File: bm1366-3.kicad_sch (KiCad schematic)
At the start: 77 parts, among them U1 25MHz, U21 TLV3544, U23 AP7331, U24 AP7331, U25 BM1368_mode1, U27 BM1368_mode1

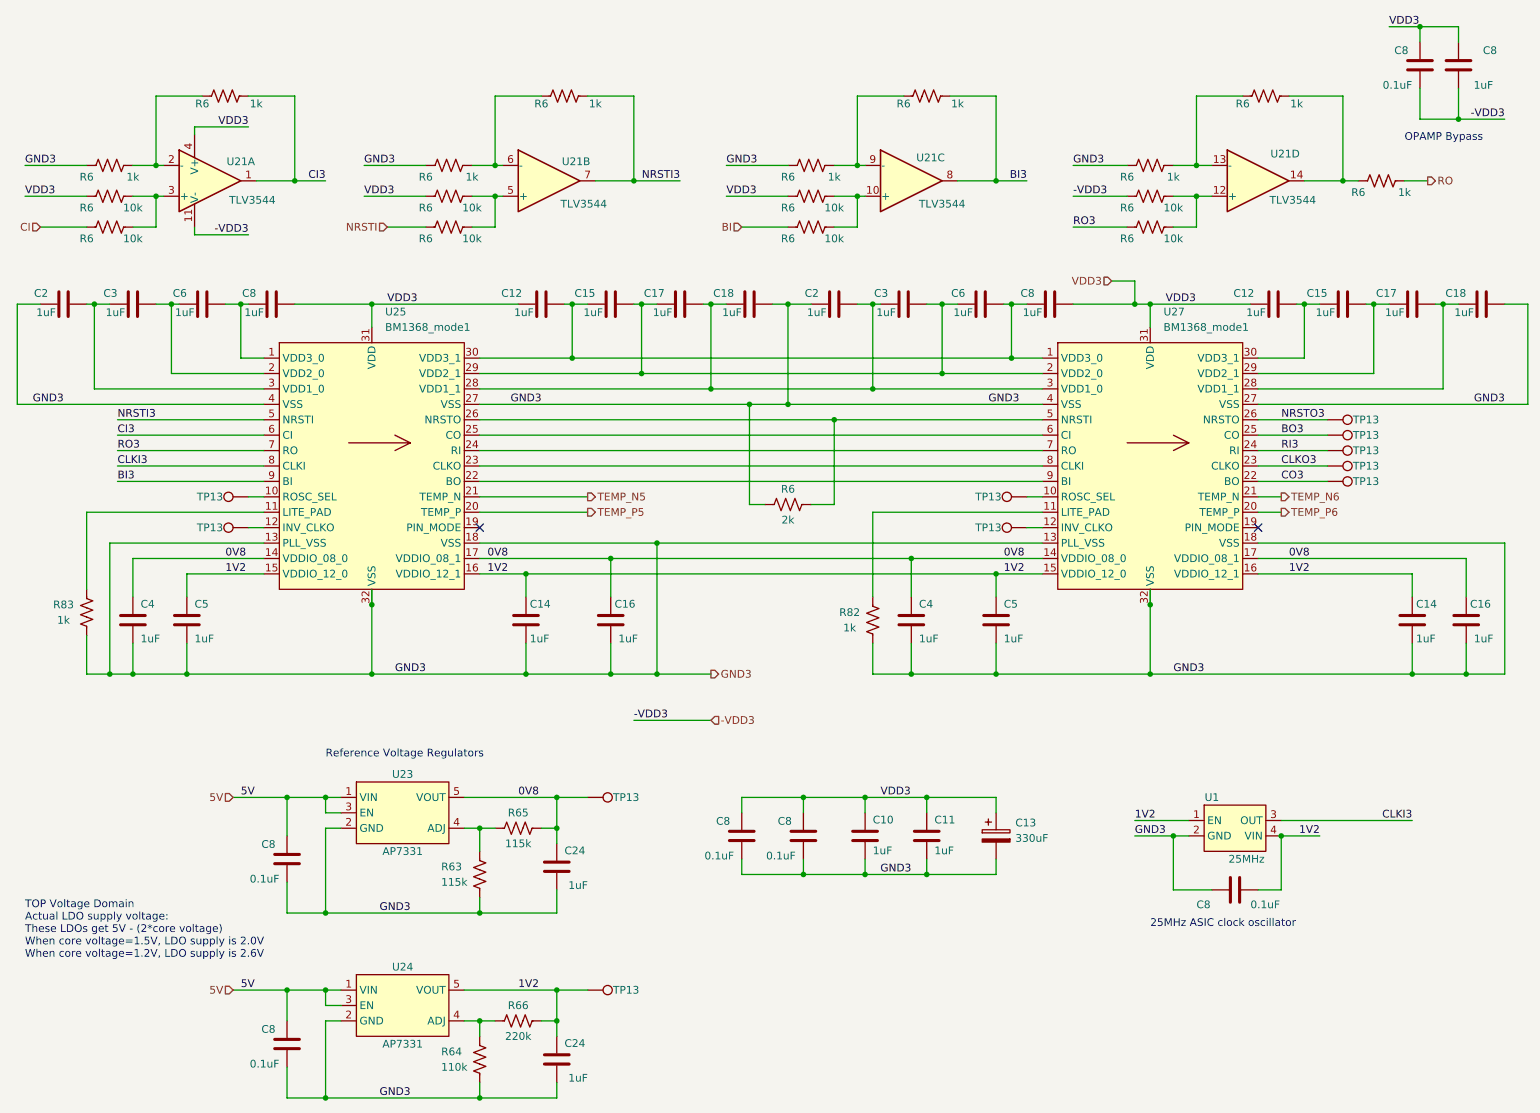
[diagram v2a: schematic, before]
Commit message: Reset to 1V8
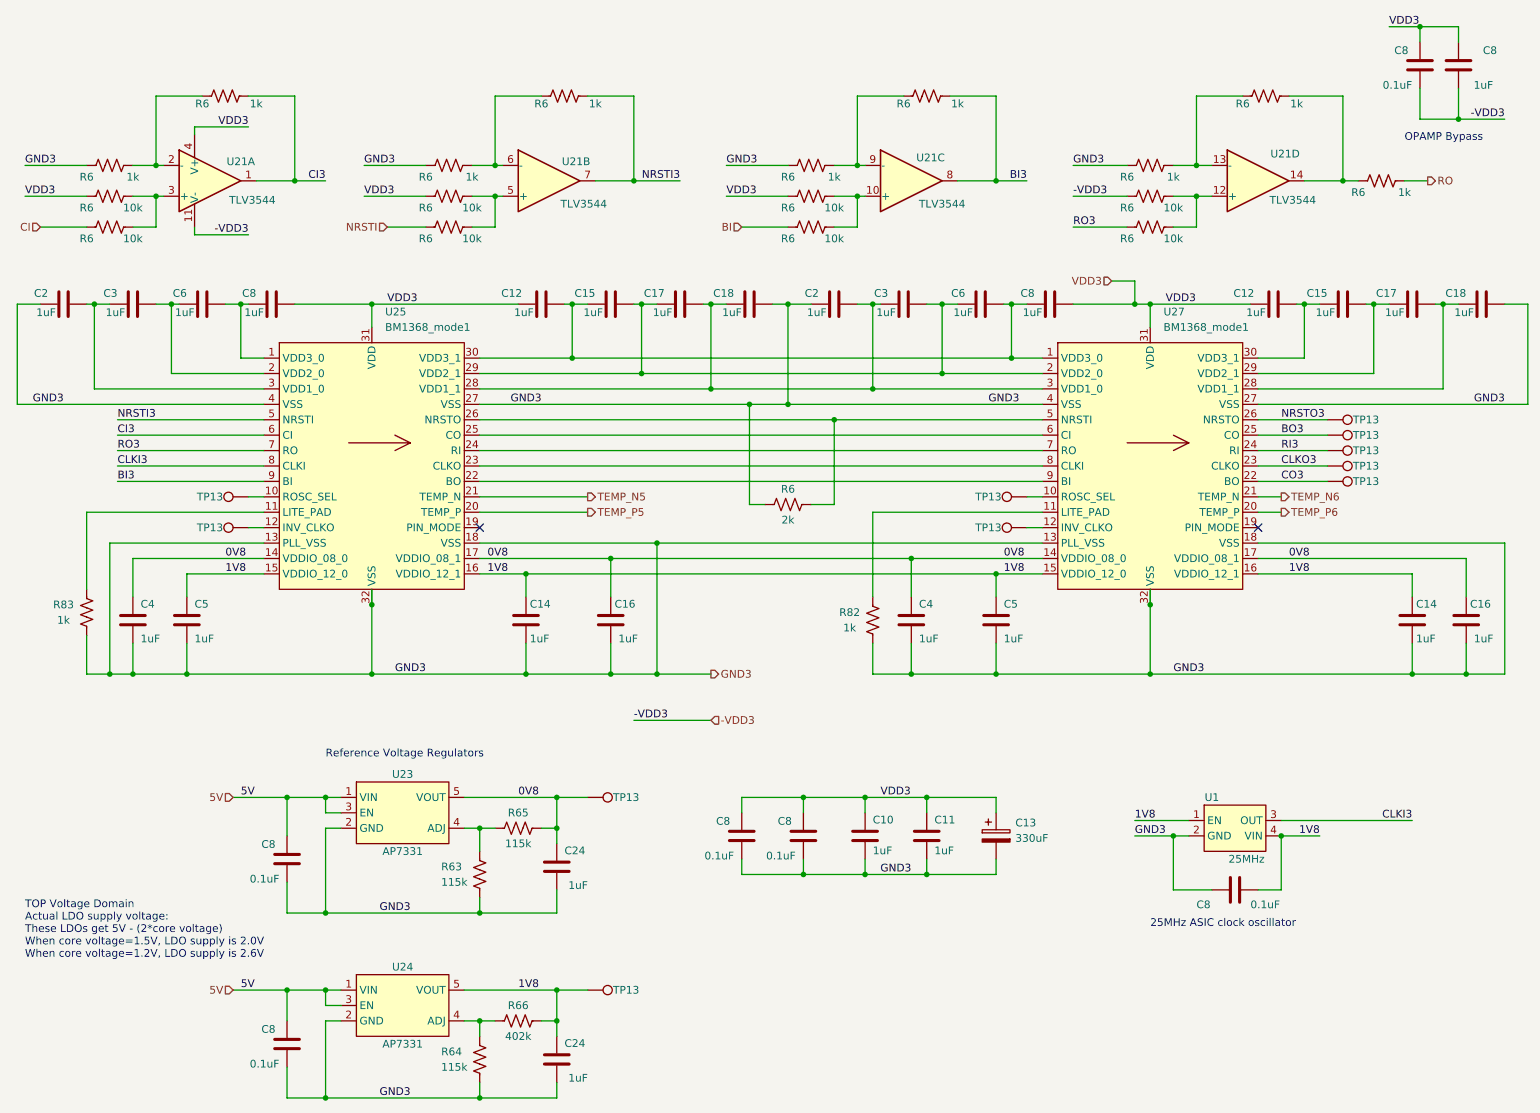
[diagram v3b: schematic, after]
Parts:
- R64: value 110k -> 115k; DK 311-110KLRTR-ND -> YAG2956CT-ND; PARTNO RC0402FR-07110KL -> RC0402FR-07115KL
- R66: value 220k -> 402k; DK 311-220KLRTR-ND -> YAG3151CT-ND; PARTNO RC0402FR-07220KL -> RC0402FR-07402KL
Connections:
- net 1V2 renamed 1V8
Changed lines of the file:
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@@
 		)
 	)
-	(label "1V2"
+	(label "1V8"
 		(at 229.87 151.13 180)
 		(fields_autoplaced yes)
@@
 		)
 	)
-	(label "1V2"
+	(label "1V8"
 		(at 49.53 107.95 0)
 		(fields_autoplaced yes)
@@
 		)
 	)
-	(label "1V2"
+	(label "1V8"
 		(at 224.79 107.95 0)
 		(fields_autoplaced yes)
@@
 		)
 	)
-	(label "1V2"
+	(label "1V8"
 		(at 92.71 107.95 0)
 		(fields_autoplaced yes)
@@
 		)
 	)
-	(label "1V2"
+	(label "1V8"
 		(at 177.8 107.95 0)
 		(fields_autoplaced yes)
@@
 		)
 	)
-	(label "1V2"
+	(label "1V8"
 		(at 199.39 148.59 0)
 		(fields_autoplaced yes)
@@
 		)
 	)
-	(label "1V2"
+	(label "1V8"
 		(at 97.79 176.53 0)
 		(fields_autoplaced yes)
@@
 	)
 	(symbol
+		(lib_id "Device:R_US")
+		(at 97.79 181.61 270)
+		(unit 1)
+		(exclude_from_sim no)
+		(in_bom yes)
+		(on_board yes)
+		(dnp no)
+		(property "Reference" "R66"
+			(at 97.79 179.07 90)
+			(effects
+				(font
+					(size 1.27 1.27)
+				)
+			)
+		)
+		(property "Value" "402k"
+			(at 97.79 184.15 90)
+			(effects
+				(font
+					(size 1.27 1.27)
+				)
+			)
+		)
+		(property "Footprint" "Resistor_SMD:R_0402_1005Metric"
+			(at 97.536 182.626 90)
+			(effects
+				(font
+					(size 1.27 1.27)
+				)
+				(hide yes)
+			)
+		)
+		(property "Datasheet" "~"
+			(at 97.79 181.61 0)
+			(effects
+				(font
+					(size 1.27 1.27)
+				)
+				(hide yes)
+			)
+		)
+		(property "Description" ""
+			(at 97.79 181.61 0)
+			(effects
+				(font
+					(size 1.27 1.27)
+				)
+				(hide yes)
+			)
+		)
+		(property "DK" "YAG3151CT-ND"
+			(at 97.79 181.61 0)
+			(effects
+				(font
+					(size 1.27 1.27)
+				)
+				(hide yes)
+			)
+		)
+		(property "PARTNO" "RC0402FR-07402KL"
+			(at 97.79 181.61 0)
+			(effects
+				(font
+					(size 1.27 1.27)
+				)
+				(hide yes)
+			)
+		)
+		(pin "1"
+		)
+		(pin "2"
+		)
+		(instances
+			(project "bitaxeHex"
+				(path "/e63e39d7-6ac0-4ffd-8aa3-1841a4541b55/e182566a-9202-4486-8792-212410a9233c"
+					(reference "R66")
+					(unit 1)
+				)
+			)
+		)
+	)
+	(symbol
 		(lib_id "Device:C")
 		(at 104.14 187.96 0)
@@
 	)
 	(symbol
-		(lib_id "Device:R_US")
-		(at 97.79 181.61 270)
-		(unit 1)
-		(exclude_from_sim no)
-		(in_bom yes)
-		(on_board yes)
-		(dnp no)
-		(property "Reference" "R66"
-			(at 97.79 179.07 90)
-			(effects
-				(font
-					(size 1.27 1.27)
-				)
-			)
-		)
-		(property "Value" "220k"
-			(at 97.79 184.15 90)
-			(effects
-				(font
-					(size 1.27 1.27)
-				)
-			)
-		)
-		(property "Footprint" "Resistor_SMD:R_0402_1005Metric"
-			(at 97.536 182.626 90)
-			(effects
-				(font
-					(size 1.27 1.27)
-				)
-				(hide yes)
-			)
-		)
-		(property "Datasheet" "~"
-			(at 97.79 181.61 0)
-			(effects
-				(font
-					(size 1.27 1.27)
-				)
-				(hide yes)
-			)
-		)
-		(property "Description" ""
-			(at 97.79 181.61 0)
-			(effects
-				(font
-					(size 1.27 1.27)
-				)
-				(hide yes)
-			)
-		)
-		(property "DK" "311-220KLRTR-ND"
-			(at 97.79 181.61 0)
-			(effects
-				(font
-					(size 1.27 1.27)
-				)
-				(hide yes)
-			)
-		)
-		(property "PARTNO" "RC0402FR-07220KL"
-			(at 97.79 181.61 0)
-			(effects
-				(font
-					(size 1.27 1.27)
-				)
-				(hide yes)
-			)
-		)
-		(pin "1"
-		)
-		(pin "2"
-		)
-		(instances
-			(project "bitaxeHex"
-				(path "/e63e39d7-6ac0-4ffd-8aa3-1841a4541b55/e182566a-9202-4486-8792-212410a9233c"
-					(reference "R66")
-					(unit 1)
-				)
-			)
-		)
-	)
-	(symbol
 		(lib_id "Device:C")
 		(at 101.6 63.5 90)
@@
 	(symbol
 		(lib_id "Device:R_US")
+		(at 91.44 187.96 180)
+		(unit 1)
+		(exclude_from_sim no)
+		(in_bom yes)
+		(on_board yes)
+		(dnp no)
+		(property "Reference" "R64"
+			(at 85.09 186.69 0)
+			(effects
+				(font
+					(size 1.27 1.27)
+				)
+				(justify right)
+			)
+		)
+		(property "Value" "115k"
+			(at 85.09 189.23 0)
+			(effects
+				(font
+					(size 1.27 1.27)
+				)
+				(justify right)
+			)
+		)
+		(property "Footprint" "Resistor_SMD:R_0402_1005Metric"
+			(at 90.424 187.706 90)
+			(effects
+				(font
+					(size 1.27 1.27)
+				)
+				(hide yes)
+			)
+		)
+		(property "Datasheet" "~"
+			(at 91.44 187.96 0)
+			(effects
+				(font
+					(size 1.27 1.27)
+				)
+				(hide yes)
+			)
+		)
+		(property "Description" ""
+			(at 91.44 187.96 0)
+			(effects
+				(font
+					(size 1.27 1.27)
+				)
+				(hide yes)
+			)
+		)
+		(property "DK" "YAG2956CT-ND"
+			(at 91.44 187.96 0)
+			(effects
+				(font
+					(size 1.27 1.27)
+				)
+				(hide yes)
+			)
+		)
+		(property "PARTNO" "RC0402FR-07115KL"
+			(at 91.44 187.96 0)
+			(effects
+				(font
+					(size 1.27 1.27)
+				)
+				(hide yes)
+			)
+		)
+		(pin "1"
+		)
+		(pin "2"
+		)
+		(instances
+			(project "bitaxeHex"
+				(path "/e63e39d7-6ac0-4ffd-8aa3-1841a4541b55/e182566a-9202-4486-8792-212410a9233c"
+					(reference "R64")
+					(unit 1)
+				)
+			)
+		)
+	)
+	(symbol
+		(lib_id "Device:R_US")
 		(at 105.41 29.21 270)
 		(unit 1)
@@
 					(unit 1)
 				)
-			)
-		)
-	)
-	(symbol
-		(lib_id "Device:R_US")
-		(at 91.44 187.96 180)
-		(unit 1)
-		(exclude_from_sim no)
-		(in_bom yes)
-		(on_board yes)
-		(dnp no)
-		(property "Reference" "R64"
-			(at 85.09 186.69 0)
-			(effects
-				(font
-					(size 1.27 1.27)
-				)
-				(justify right)
-			)
-		)
-		(property "Value" "110k"
-			(at 85.09 189.23 0)
-			(effects
-				(font
-					(size 1.27 1.27)
-				)
-				(justify right)
-			)
-		)
-		(property "Footprint" "Resistor_SMD:R_0402_1005Metric"
-			(at 90.424 187.706 90)
-			(effects
-				(font
-					(size 1.27 1.27)
-				)
-				(hide yes)
-			)
-		)
-		(property "Datasheet" "~"
-			(at 91.44 187.96 0)
-			(effects
-				(font
-					(size 1.27 1.27)
-				)
-				(hide yes)
-			)
-		)
-		(property "Description" ""
-			(at 91.44 187.96 0)
-			(effects
-				(font
-					(size 1.27 1.27)
-				)
-				(hide yes)
-			)
-		)
-		(property "DK" "311-110KLRTR-ND"
-			(at 91.44 187.96 0)
-			(effects
-				(font
-					(size 1.27 1.27)
-				)
-				(hide yes)
-			)
-		)
-		(property "PARTNO" "RC0402FR-07110KL"
-			(at 91.44 187.96 0)
-			(effects
-				(font
-					(size 1.27 1.27)
-				)
-				(hide yes)
-			)
-		)
-		(pin "1"
-		)
-		(pin "2"
-		)
-		(instances
-			(project "bitaxeHex"
-				(path "/e63e39d7-6ac0-4ffd-8aa3-1841a4541b55/e182566a-9202-4486-8792-212410a9233c"
-					(reference "R64")
-					(unit 1)
-				)

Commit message: init push for GammaHex
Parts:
- removed U25, U27: BM1368_mode1, bitaxe:BM1368, symbol bitaxe:BM1368_mode1
- added U25, U27: BM1370_mode1, bitaxe:BM1370, symbol bitaxe:BM1370_mode1
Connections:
- net 0V8: now also U25.14 (VDDIO_08_0), U25.17 (VDDIO_08_1), U27.14 (VDDIO_08_0), U27.17 (VDDIO_08_1)
- net 1V8: now also U25.15 (VDDIO_12_0), U25.16 (VDDIO_12_1), U27.15 (VDDIO_12_0), U27.16 (VDDIO_12_1)
- net BI3: now also U25.9 (BI)
- net BO3: now also U27.25 (CO)
- net CI3: now also U25.6 (CI)
- net CLKI3: now also U25.8 (CLKI)
- net CLKO3: now also U27.23 (CLKO)
- net CO3: now also U27.22 (BO)
- net GND3: now also U25.13 (PLL_VSS), U25.18 (VSS), U25.27 (VSS), U25.32 (VSS), U25.4 (VSS), U27.13 (PLL_VSS), U27.18 (VSS), U27.27 (VSS), U27.32 (VSS), U27.4 (VSS)
- net NRSTI3: now also U25.5 (NRSTI)
- net NRSTO3: now also U27.26 (NRSTO)
- net RI3: now also U27.24 (RI)
- net RO3: now also U25.7 (RO)
- net TEMP_N5: now also U25.21 (TEMP_N)
- net TEMP_N6: now also U27.21 (TEMP_N)
- net TEMP_P5: now also U25.20 (TEMP_P)
- net TEMP_P6: now also U27.20 (TEMP_P)
- net VDD3: now also U25.31 (VDD), U27.31 (VDD)
- net at C17.2, C18.1: now also U27.28 (VDD1_1)
- net at C12.2, C15.1: now also U27.30 (VDD3_1)
- net at C6.2, C8.1: now also U25.1 (VDD3_0)
- net at C17.2, C18.1, C2.2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: now also U25.28 (VDD1_1), U27.3 (VDD1_0)
- net at C15.2, C17.1, C3.2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: now also U25.29 (VDD2_1), U27.2 (VDD2_0)
- net at C12.2, C15.1, C6.2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: now also U25.30 (VDD3_1), U27.1 (VDD3_0)
- net at R6.2: now also U25.26 (NRSTO), U27.5 (NRSTI)
- net at C15.2, C17.1: now also U27.29 (VDD2_1)
- net at C3.2, C6.1: now also U25.2 (VDD2_0)
- net at R83.2: now also U25.11 (LITE_PAD)
- net at TP13.1: now also U27.10 (ROSC_SEL)
- net at R82.2: now also U27.11 (LITE_PAD)
- net at TP13.1: now also U27.12 (INV_CLKO)
- net at TP13.1: now also U25.10 (ROSC_SEL)
- net at TP13.1: now also U25.12 (INV_CLKO)
- net at C2.2, C3.1: now also U25.3 (VDD1_0)
- new net: U25.25 (CO), U27.6 (CI)
- new net: U25.24 (RI), U27.7 (RO)
- new net: U25.23 (CLKO), U27.8 (CLKI)
- new net: U25.22 (BO), U27.9 (BI)
